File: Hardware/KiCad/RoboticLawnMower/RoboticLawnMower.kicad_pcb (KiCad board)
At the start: 2 copper layers, 100.1 x 100 mm, 117 parts, among them J1 MOTOR, J10 Conn_01x02, J11 Conn_01x02, J12 Conn_02x05_Row_Letter_Last, J13 I2C 0, J14 ADC 1, J15 ADC 2, J16 Conn_01x03, J17 Conn_01x03, J18 Conn_01x03, J19 RAIN, J2 MOTOR, J20 Dist 00, J21 Dist 01, J22 Dist 02, J3 MOTOR, J4 MOTOR, J5 MOTOR, J6 Coll 00, J7 Coll 01, J8 Coll 02, J9 GPS, Q1 BSS123, Q2 BSS123, Q3 Si7141DP, Q4 Si7141DP, U1 INA233, U10 INA233, U11 INA233, U12 INA233, U13 INA233, U2 AVR128DB48x-xPT, U3 mini_esp32, U4 PCA9685PW, U6 LT1129-3.3_SOT223, U7 TSR_1-2450, U8 ADS1115IDGS, U9 ADS1115IDGS, Y1 32.768kHz

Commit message: Layout ready add gerber file
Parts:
- removed J10: Conn_01x02, Connector_Phoenix_MC:PhoenixContact_MCV_1,5_2-GF-3.81_1x02_P3.81mm_Vertical_ThreadedFlange_MountHole
- added C11: 100n, Capacitor_SMD:C_0603_1608Metric, F.Cu at (124.2, 101.3)
- added C13: 100n, Capacitor_SMD:C_0603_1608Metric, F.Cu at (124.2, 98.6)
- added C23: 100n, Capacitor_SMD:C_0603_1608Metric, F.Cu at (124.2, 96.9)
- added C24: 100n, Capacitor_SMD:C_0603_1608Metric, F.Cu at (130.4, 101.7)
- added C34: 1u, Capacitor_SMD:C_0603_1608Metric, F.Cu at (130.4, 103.5)
- added H6: MountingHole, MountingHole:MountingHole_3.2mm_M3, F.Cu at (185.5, 80.0)
- added Q5: Si7141DP, Package_SO:PowerPAK_SO-8_Single, F.Cu at (99.1, 57.4)
- added Q6: BSS123, Package_TO_SOT_SMD:SOT-23, F.Cu at (100.7, 62.0)
- added R19: 4k7, Resistor_SMD:R_0603_1608Metric, F.Cu at (139.3, 106.2)
- added R20: 4k7, Resistor_SMD:R_0603_1608Metric, F.Cu at (137.5, 106.2)
- added R21: 4k7, Resistor_SMD:R_0603_1608Metric, F.Cu at (135.0, 106.2)
- added R22: 1K, Resistor_SMD:R_0603_1608Metric, F.Cu at (97.2, 62.0)
- added R23: 100k, Resistor_SMD:R_0603_1608Metric, F.Cu at (94.1, 58.8)
- added R24: 1M, Resistor_SMD:R_0603_1608Metric, F.Cu at (103.6, 62.0)
- added R25: 100R, Resistor_SMD:R_0603_1608Metric, F.Cu at (103.6, 65.0)
- added U5: W25Q128JVS, Package_SO:SOIC-8_5.23x5.23mm_P1.27mm, F.Cu at (136.9, 101.5)
- moved H5 47.6 mm to (92.4, 90.8)
- moved R42 16.0 mm to (127.4, 108.7)
- moved R41 15.9 mm to (127.4, 107.1)
- moved U7 14.7 mm to (95.2, 107.0)
- moved C15 4.96 mm to (105.1, 111.1)
- moved C16 4.96 mm to (105.0, 109.3)
- moved C17 4.78 mm to (105.0, 98.2)
- moved U6 4.78 mm to (103.0, 104.5)
- moved C18 4.78 mm to (105.0, 99.9)
- moved C25 3.94 mm to (140.3, 82.2), turned to 90 degrees
- moved R26 2.01 mm to (126.6, 79.1)
- moved R27 2.01 mm to (137.0, 82.2)
- moved U2 2.01 mm to (129.7, 91.8)
- moved J12 2.01 mm to (131.7, 81.4)
- moved R28 1.89 mm to (138.7, 82.2)
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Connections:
- J9 pad 7: unconnected-(J9-Pad7) -> /GPS/GPS_MOD_EN
- U2 pad 12: /i2c_io_pwm/~{PCA_9685_OE} -> /Motor_M5_EN
- U2 pad 16: /Motor_M5_EN -> /i2c_io_pwm/~{PCA_9685_OE}
- U2 pad 20: unconnected-(U2-Pad20) -> /Motor_M2/MOT_SIGNAL
- U2 pad 4: unconnected-(U2-Pad4) -> /WLAN/WLAN_MOD_EN
- U2 pad 44: unconnected-(U2-Pad44) -> /Motor_M1/MOT_SIGNAL
- U2 pad 5: unconnected-(U2-Pad5) -> /GPS/GPS_MOD_EN
- U3 pad 16: +3.3V -> Net-(U3-Pad16)
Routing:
- net +3.3V: track 160.1 -> 486.1 mm, vias 12 -> 14
- net GND: track 393.8 -> 620.9 mm, vias 10 -> 13
- net /Sensor/Collision_Sensor_00: track 0.00 -> 73.0 mm, vias 0 -> 1
- net /i2c_analog/SCL: track 4.55 -> 72.4 mm, vias 1 -> 0
- net /Sensor/Collision_Sensor_01: track 0.00 -> 64.7 mm, vias 0 -> 1
- net /Sensor/Collision_Sensor_02: track 0.00 -> 63.2 mm, vias 0 -> 1
- net /i2c_analog/SDA: track 5.48 -> 65.3 mm, vias 1 -> 0
- net /Sensor/DistanceSensor_00: track 0.00 -> 44.8 mm
- net /WLAN/WLAN_MOD_EN: track 0.00 -> 41.1 mm
- net /Sensor/RainSensor: track 0.00 -> 41.0 mm
- net /Sensor/DistanceSensor_02: track 0.00 -> 37.3 mm
- net /GPS/GPS_MOD_EN: track 0.00 -> 32.6 mm
- net /Motor_M2/MOT_SIGNAL: track 32.0 -> 62.3 mm, vias 1 -> 3
- net /Sensor/DistanceSensor_01: track 0.00 -> 28.1 mm
- net /Motor_M1/MOT_SIGNAL: track 45.7 -> 73.6 mm, vias 1 -> 3
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- added copper zone on B.Cu, net GND
- added copper zone on F.Cu, net GND
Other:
- board text added: "3V3 AIN 0 AIN 1 AIN 2 AIN 3 GND"
- board text added: "3V3 GND Sig"
- board text added: "3V3 GND TXD RXD RES PPS POW_EN"
- board text added: "3V3 SCL SDA GND"
- board text added: "DBG/PROG"
- board text added: "GPS"
- board text added: "MOTOR"
- board text added: "POWER + - 12-24V"
- board text added: "U+ GND N.C. EN SIG PWM 0 PWM 1 GND"
- board text added: "WLAN-ESP32 WEMOS D1"

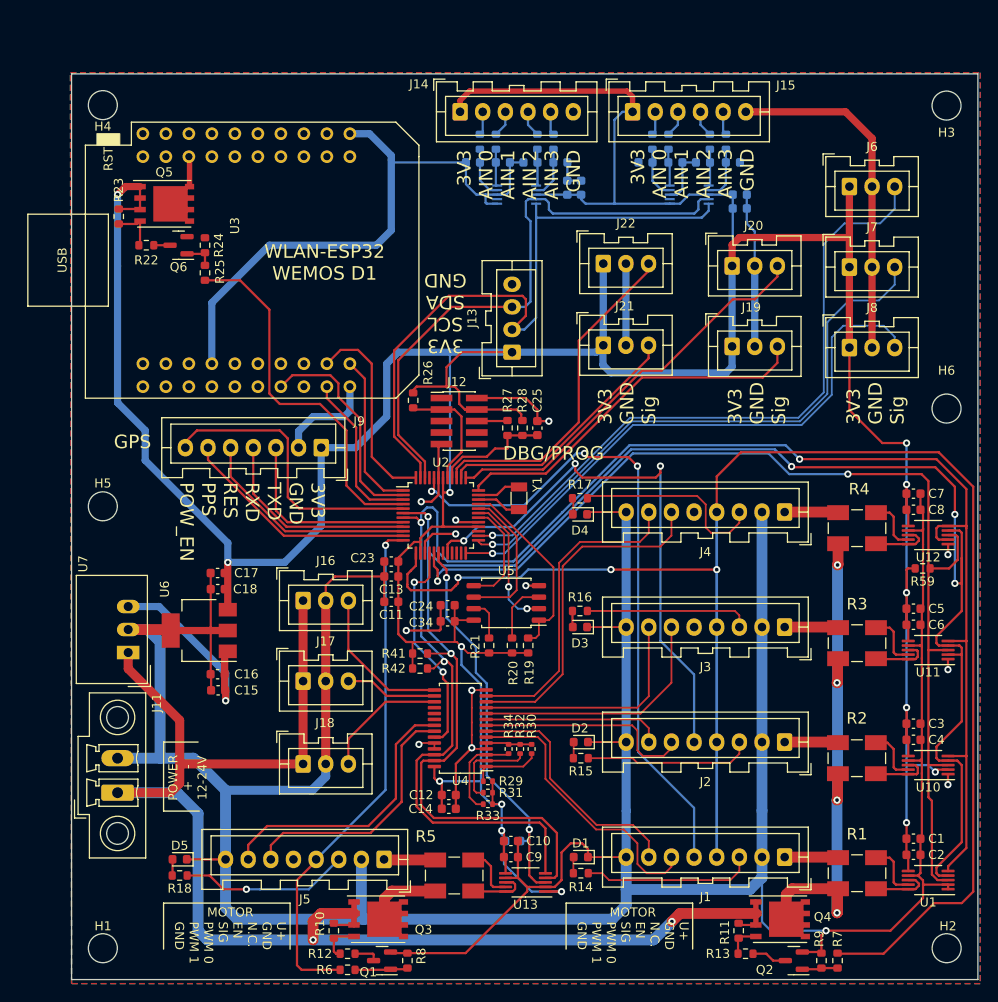
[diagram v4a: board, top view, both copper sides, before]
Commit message: Redesign: - Controller - I2C pinning geändert - uvm
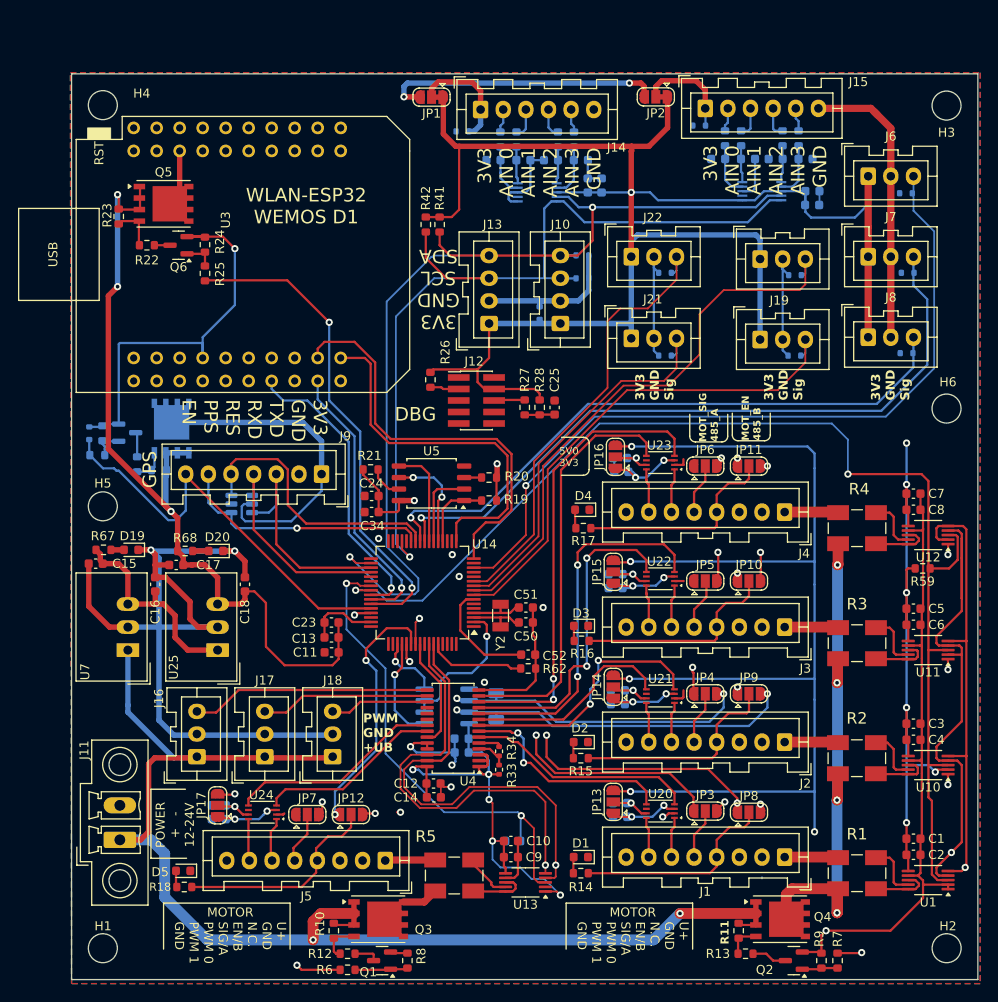
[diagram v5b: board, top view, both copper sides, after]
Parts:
- removed R29, R31: 10K, Resistor_SMD:R_0402_1005Metric
- removed R30, R32: N.P., Resistor_SMD:R_0402_1005Metric
- removed Y1: 32.768kHz, Crystal:Crystal_SMD_3215-2Pin_3.2x1.5mm
- added C35: 100n, Capacitor_SMD:C_0603_1608Metric, B.Cu at (149.5, 125.1)
- added C36: 100n, Capacitor_SMD:C_0603_1608Metric, B.Cu at (149.2, 112.6)
- added C37: 100n, Capacitor_SMD:C_0603_1608Metric, B.Cu at (149.0, 99.8)
- added C38: 100n, Capacitor_SMD:C_0603_1608Metric, B.Cu at (149.6, 87.0)
- added C39: 100n, Capacitor_SMD:C_0603_1608Metric, B.Cu at (105.2, 125.3)
- added C45: 100n, Capacitor_SMD:C_0603_1608Metric, B.Cu at (149.5, 123.6)
- added C46: 100n, Capacitor_SMD:C_0603_1608Metric, B.Cu at (149.2, 111.1)
- added C47: 100n, Capacitor_SMD:C_0603_1608Metric, B.Cu at (149.0, 98.3)
- added C48: 100n, Capacitor_SMD:C_0603_1608Metric, B.Cu at (149.5, 85.5)
- added C49: 100n, Capacitor_SMD:C_0603_1608Metric, B.Cu at (105.2, 123.8)
- added C50: Cx, Capacitor_SMD:C_0603_1608Metric, F.Cu at (139.1, 103.6)
- added C51: Cx, Capacitor_SMD:C_0603_1608Metric, F.Cu at (139.1, 102.0)
- added C52: 100n, Capacitor_SMD:C_0603_1608Metric, F.Cu at (139.3, 107.2)
- added C53: 100n, Capacitor_SMD:C_0603_1608Metric, B.Cu at (132.0, 116.5)
- added C54: 1u, Capacitor_SMD:C_0603_1608Metric, B.Cu at (132.0, 118.0)
- added D10: ESD5Zxx, Diode_SMD:D_SOD-523, B.Cu at (181.1, 73.9)
- added D11: ESD5Zxx, Diode_SMD:D_SOD-523, B.Cu at (181.2, 65.0)
- added D12: ESD5Zxx, Diode_SMD:D_SOD-523, B.Cu at (181.0, 56.2)
- added D13: ESD5Zxx, Diode_SMD:D_SOD-523, B.Cu at (132.1, 49.4)
- added D14: ESD5Zxx, Diode_SMD:D_SOD-523, B.Cu at (158.2, 48.8)
- added D15: ESD5Zxx, Diode_SMD:D_SOD-523, B.Cu at (145.3, 65.6)
- added D16: ESD5Zxx, Diode_SMD:D_SOD-523, B.Cu at (145.3, 63.1)
- added D17: ESD5Zxx, Diode_SMD:D_SOD-523, B.Cu at (140.6, 69.5)
- added D18: ESD5Zxx, Diode_SMD:D_SOD-523, B.Cu at (90.9, 82.7)
- added D19: LED_GREEN, LED_SMD:LED_0603_1608Metric, F.Cu at (95.5, 95.6)
- added D20: LED_GREEN, LED_SMD:LED_0603_1608Metric, F.Cu at (104.8, 95.7)
- added D6: ESD5Zxx, Diode_SMD:D_SOD-523, B.Cu at (168.7, 74.2)
- added D7: ESD5Zxx, Diode_SMD:D_SOD-523, B.Cu at (168.8, 65.3)
- added D8: ESD5Zxx, Diode_SMD:D_SOD-523, B.Cu at (154.4, 74.2)
- added D9: ESD5Zxx, Diode_SMD:D_SOD-523, B.Cu at (154.4, 65.0)
- added J10: I2C 0, Connector_JST:JST_XA_B04B-XASK-1_1x04_P2.50mm_Vertical, F.Cu at (142.9, 70.6)
- added JP1: Jumper_3_Open, Jumper:SolderJumper-3_P1.3mm_Bridged12_RoundedPad1.0x1.5mm, F.Cu at (128.7, 45.6)
- added JP10: SolderJumper_3_Open, Jumper:SolderJumper-3_P1.3mm_Open_RoundedPad1.0x1.5mm, F.Cu at (163.7, 99.1)
- added JP11: SolderJumper_3_Open, Jumper:SolderJumper-3_P1.3mm_Open_RoundedPad1.0x1.5mm, F.Cu at (163.7, 86.4)
- added JP12: SolderJumper_3_Open, Jumper:SolderJumper-3_P1.3mm_Open_RoundedPad1.0x1.5mm, F.Cu at (119.8, 124.8)
- added JP13: SolderJumper_3_Open, Jumper:SolderJumper-3_P1.3mm_Open_RoundedPad1.0x1.5mm, F.Cu at (148.7, 123.4)
- added JP14: SolderJumper_3_Open, Jumper:SolderJumper-3_P1.3mm_Open_RoundedPad1.0x1.5mm, F.Cu at (148.7, 110.7)
- added JP15: SolderJumper_3_Open, Jumper:SolderJumper-3_P1.3mm_Open_RoundedPad1.0x1.5mm, F.Cu at (148.7, 98.0)
- added JP16: SolderJumper_3_Open, Jumper:SolderJumper-3_P1.3mm_Open_RoundedPad1.0x1.5mm, F.Cu at (149.0, 85.3)
- added JP17: SolderJumper_3_Open, Jumper:SolderJumper-3_P1.3mm_Open_RoundedPad1.0x1.5mm, F.Cu at (105.0, 123.8)
- added JP2: Jumper_3_Open, Jumper:SolderJumper-3_P1.3mm_Bridged12_RoundedPad1.0x1.5mm, F.Cu at (153.4, 45.6)
- added JP3: SolderJumper_3_Open, Jumper:SolderJumper-3_P1.3mm_Open_RoundedPad1.0x1.5mm, F.Cu at (158.9, 124.5)
- added JP4: SolderJumper_3_Open, Jumper:SolderJumper-3_P1.3mm_Open_RoundedPad1.0x1.5mm, F.Cu at (158.9, 111.5)
- added JP5: SolderJumper_3_Open, Jumper:SolderJumper-3_P1.3mm_Open_RoundedPad1.0x1.5mm, F.Cu at (158.9, 99.1)
- added JP6: SolderJumper_3_Open, Jumper:SolderJumper-3_P1.3mm_Open_RoundedPad1.0x1.5mm, F.Cu at (158.9, 86.4)
- added JP7: SolderJumper_3_Open, Jumper:SolderJumper-3_P1.3mm_Open_RoundedPad1.0x1.5mm, F.Cu at (114.9, 124.8)
- added JP8: SolderJumper_3_Open, Jumper:SolderJumper-3_P1.3mm_Open_RoundedPad1.0x1.5mm, F.Cu at (163.7, 124.6)
- added JP9: SolderJumper_3_Open, Jumper:SolderJumper-3_P1.3mm_Open_RoundedPad1.0x1.5mm, F.Cu at (163.7, 111.5)
- added Q7: Si7141DP, Package_SO:PowerPAK_SO-8_Single, B.Cu at (99.9, 82.2)
- added Q8: BSS123, Package_TO_SOT_SMD:SOT-23, B.Cu at (95.0, 82.7)
- added R62: 47K, Resistor_SMD:R_0603_1608Metric, F.Cu at (139.3, 108.7)
- added R63: 1K, Resistor_SMD:R_0603_1608Metric, B.Cu at (96.1, 86.2)
- added R64: 100k, Resistor_SMD:R_0603_1608Metric, B.Cu at (98.6, 86.8)
- added R65: 1M, Resistor_SMD:R_0603_1608Metric, B.Cu at (92.3, 82.7)
- added R66: 100R, Resistor_SMD:R_0603_1608Metric, B.Cu at (91.7, 85.2)
- added R67: 4k7, Resistor_SMD:R_0603_1608Metric, F.Cu at (92.4, 95.6)
- added R68: 4k7, Resistor_SMD:R_0603_1608Metric, F.Cu at (101.4, 95.7)
- added R69: 120, Resistor_SMD:R_1206_3216Metric, B.Cu at (135.8, 112.9)
- added U14: STM32H503RBTx, Package_QFP:LQFP-64_10x10mm_P0.5mm, F.Cu at (127.6, 100.3)
- added U20: TXB0102DCU, Package_SO:VSSOP-8_2.4x2.1mm_P0.5mm, F.Cu at (153.9, 124.5)
- added U21: TXB0102DCU, Package_SO:VSSOP-8_2.4x2.1mm_P0.5mm, F.Cu at (153.9, 111.8)
- added U22: TXB0102DCU, Package_SO:VSSOP-8_2.4x2.1mm_P0.5mm, F.Cu at (153.9, 98.8)
- added U23: TXB0102DCU, Package_SO:VSSOP-8_2.4x2.1mm_P0.5mm, F.Cu at (153.9, 86.0)
- added U24: TXB0102DCU, Package_SO:VSSOP-8_2.4x2.1mm_P0.5mm, F.Cu at (110.0, 124.6)
- added U25: TSR_1-2450, Converter_DCDC:Converter_DCDC_TRACO_TSR-1_THT, F.Cu at (105.0, 106.7)
- added Y2: 32.768kHz, Crystal:Crystal_SMD_3215-2Pin_3.2x1.5mm, F.Cu at (136.3, 102.9)
- R33: value 10K -> N.P.
- R34: value N.P. -> 0R0
- U2: value AVR128DB48x-xPT -> LT1785AxS8; footprint Package_QFP:TQFP-48_7x7mm_P0.5mm -> Package_SO:SOIC-8_3.9x4.9mm_P1.27mm; moved to B.Cu
- U6: value LT1129-3.3_SOT223 -> SRV05-4; footprint Package_TO_SOT_SMD:SOT-223-3_TabPin2 -> Package_TO_SOT_SMD:SOT-23-6; moved to B.Cu
- moved R42 49.0 mm to (128.0, 59.7), turned to 90 degrees
- moved R41 47.4 mm to (129.5, 59.7), turned to 90 degrees
- moved R21 23.4 mm to (121.9, 86.7), turned to 180 degrees
- moved U2 21.1 mm to (130.3, 112.9)
- moved J16 20.8 mm to (102.7, 118.5), turned to 90 degrees
- moved C15 19.5 mm to (91.6, 97.1)
- moved R20 18.7 mm to (135.0, 87.6), turned to 0 degrees
- moved R19 16.6 mm to (135.0, 90.2), turned to 0 degrees
- moved U5 15.6 mm to (128.7, 88.3)
- moved U6 14.7 mm to (107.7, 90.6), turned to 0 degrees
- moved C24 14.7 mm to (122.0, 89.7)
- moved C34 14.7 mm to (122.0, 91.4)
- moved C16 12.1 mm to (98.1, 99.4), turned to 90 degrees
- moved C23 9.43 mm to (117.6, 103.6)
- moved C13 9.43 mm to (117.6, 105.3)
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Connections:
- J1 pad 4: /Motor_M1..4_EN -> Net-(J1-Pin_4)
- J1 pad 5: /Motor_M1/MOT_SIGNAL -> Net-(J1-Pin_5)
- J1 pad 6: /PWM_CH_0 -> Net-(J1-Pin_6)
- J1 pad 7: /PWM_CH_1 -> Net-(J1-Pin_7)
- J13 pad 2: /i2c_analog/SCL -> GND
- J13 pad 3: /i2c_analog/SDA -> /i2c_analog/I2C_2_SCL
- J13 pad 4: GND -> /i2c_analog/I2C_2_SDA
- J14 pad 1: +3.3V -> Net-(D13-K)
- J15 pad 1: +3.3V -> Net-(D14-K)
- J2 pad 4: /Motor_M1..4_EN -> Net-(J2-Pin_4)
- J2 pad 5: /Motor_M2/MOT_SIGNAL -> Net-(J2-Pin_5)
- J2 pad 6: /PWM_CH_2 -> Net-(J2-Pin_6)
- J2 pad 7: /PWM_CH_3 -> Net-(J2-Pin_7)
- J3 pad 4: /Motor_M1..4_EN -> Net-(J3-Pin_4)
- J3 pad 5: /Motor_M3/MOT_SIGNAL -> Net-(J3-Pin_5)
- J3 pad 6: /PWM_CH_4 -> Net-(J3-Pin_6)
- J3 pad 7: /PWM_CH_5 -> Net-(J3-Pin_7)
- J4 pad 4: /Motor_M1..4_EN -> Net-(J4-Pin_4)
- J4 pad 5: /Motor_M4/MOT_SIGNAL -> Net-(J4-Pin_5)
- J4 pad 6: /PWM_CH_6 -> Net-(J4-Pin_6)
- J4 pad 7: /PWM_CH_7 -> Net-(J4-Pin_7)
- J5 pad 4: /Motor_M5_EN -> Net-(J5-Pin_4)
- J5 pad 5: /Motor_M5/MOT_SIGNAL -> Net-(J5-Pin_5)
- J5 pad 6: /PWM_CH_15 -> Net-(J5-Pin_6)
- J5 pad 7: /PWM_CH_14 -> Net-(J5-Pin_7)
- J6 pad 3: /Sensor/Collision_Sensor_00 -> /uC/ADC_1_IN0
- J7 pad 3: /Sensor/Collision_Sensor_01 -> /uC/ADC_1_IN4
- J8 pad 3: /Sensor/Collision_Sensor_02 -> /uC/ADC_1_IN8
- J9 pad 1: +3.3V -> Net-(J9-Pin_1)
- J9 pad 3: /GPS/GPS_UART_3_TXD -> /uC/USART_1_TX
- J9 pad 4: /GPS/GPS_UART_3_RXD -> /uC/USART_1_RX
- R14 pad 1: /Motor_M1/MOT_5V_OUT -> Net-(J1-Pin_4)
- R15 pad 1: /Motor_M2/MOT_5V_OUT -> Net-(J2-Pin_4)
- R16 pad 1: /Motor_M3/MOT_5V_OUT -> Net-(J3-Pin_4)
- R17 pad 1: /Motor_M4/MOT_5V_OUT -> Net-(J4-Pin_4)
- R18 pad 1: /Motor_M5/MOT_5V_OUT -> Net-(J5-Pin_4)
- R19 pad 1: /uC/SPI_0_CS -> /uC/SPI_1_CS
- R33 pad 2: Net-(R33-Pad2) -> Net-(U4-A3)
- R34 pad 1: Net-(R33-Pad2) -> Net-(U4-A3)
- R41 pad 1: /Motor_M1/SDA -> /i2c_analog/I2C_2_SDA
- R42 pad 1: /Motor_M1/SCL -> /i2c_analog/I2C_2_SCL
- U2 pad 1: /WLAN/WLAN_TxD -> /uC/USART_3_RX
- U2 pad 2: /WLAN/UART_0_XCK -> /RS485/RS485_DIR
- U2 pad 3: /WLAN/UART_0_XDIR -> /RS485/RS485_DIR
- U2 pad 4: /WLAN/WLAN_MOD_EN -> /uC/USART_3_TX
- U2 pad 5: /GPS/GPS_MOD_EN -> GND
- U2 pad 6: /Motor_M1/SDA -> /RS485_A
- U2 pad 7: /Motor_M1/SCL -> /RS485_B
- U2 pad 8: /GPS/GPS_UART_3_TXD -> +3.3V
- U3 pad 21: /WLAN/WLAN_TxD -> /uC/USART_2_RX
- U3 pad 23: /WLAN/WLAN_RxD -> /uC/USART_2_TX
- U4 pad 1: Net-(R29-Pad2) -> +3.3V
- U4 pad 2: Net-(R31-Pad2) -> +3.3V
- U4 pad 3: Net-(R33-Pad2) -> +3.3V
- U4 pad 4: GND -> Net-(U4-A3)
- U5 pad 1: /uC/SPI_0_CS -> /uC/SPI_1_CS
- U5 pad 2: /uC/SPI_0_MISO -> /uC/SPI_1_MISO
- U5 pad 5: /uC/SPI_0_MOSI -> /uC/SPI_1_MOSI
- U5 pad 6: /uC/SPI_0_SCLK -> /uC/SPI_1_SCK
- U6 pad 1: +5V -> /GPS/GPS_PPS
- U6 pad 3: +3.3V -> /GPS/GPS_RESET_EN
- U8 pad 10: /i2c_analog/SCL -> /i2c_analog/I2C_2_SCL
- U8 pad 9: /i2c_analog/SDA -> /i2c_analog/I2C_2_SDA
- U9 pad 10: /i2c_analog/SCL -> /i2c_analog/I2C_2_SCL
- U9 pad 9: /i2c_analog/SDA -> /i2c_analog/I2C_2_SDA
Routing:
- net +5V: track 22.4 -> 363.8 mm, vias 1 -> 9
- net GND: track 620.9 -> 357.4 mm, vias 13 -> 16
- net /i2c_analog/I2C_2_SDA: track 0.00 -> 109.6 mm, vias 0 -> 2
- net /RS485_B: track 0.00 -> 104.4 mm, vias 0 -> 6
- net /RS485_A: track 0.00 -> 100.9 mm, vias 0 -> 6
- net /i2c_analog/I2C_2_SCL: track 0.00 -> 97.9 mm, vias 0 -> 1
- net /uC/ADC_1_IN0: track 0.00 -> 85.3 mm, vias 0 -> 1
- net /uC/ADC_1_IN4: track 0.00 -> 78.2 mm, vias 0 -> 1
- net /Sensor/Collision_Sensor_00: track 73.0 -> 0.00 mm, vias 1 -> 0
- net /i2c_analog/SCL: track 72.4 -> 0.00 mm
- net /uC/ADC_1_IN8: track 0.00 -> 69.0 mm, vias 0 -> 1
- net /i2c_analog/SDA: track 65.3 -> 0.00 mm
- net /Sensor/Collision_Sensor_01: track 64.7 -> 0.00 mm, vias 1 -> 0
- net /Sensor/Collision_Sensor_02: track 63.2 -> 0.00 mm, vias 1 -> 0
- net /Motor_M1..4_EN: track 175.3 -> 124.7 mm, vias 3 -> 7
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- added copper zone on In1.Cu, net +3.3V
- added copper zone on In2.Cu, net GND
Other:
- copper layers 2 -> 4
- board text added: "3V3 GND SCL SDA"
- board text added: "3V3 GND TXD RXD RES PPS EN"
- board text added: "5V0 3V3"
- board text added: "DBG"
- board text added: "MOT_EN 485_B"
- board text added: "MOT_SIG 485_A"
- board text added: "PWM GND +UB"
- board text added: "U+ GND N.C. EN/B SIG/A PWM 0 PWM 1 GND"
- board text removed: "3V3 GND TXD RXD RES PPS POW_EN"
- board text removed: "3V3 SCL SDA GND"
- board text removed: "DBG/PROG"
- board text removed: "U+ GND N.C. EN SIG PWM 0 PWM 1 GND"

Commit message: change µC to STM32H573
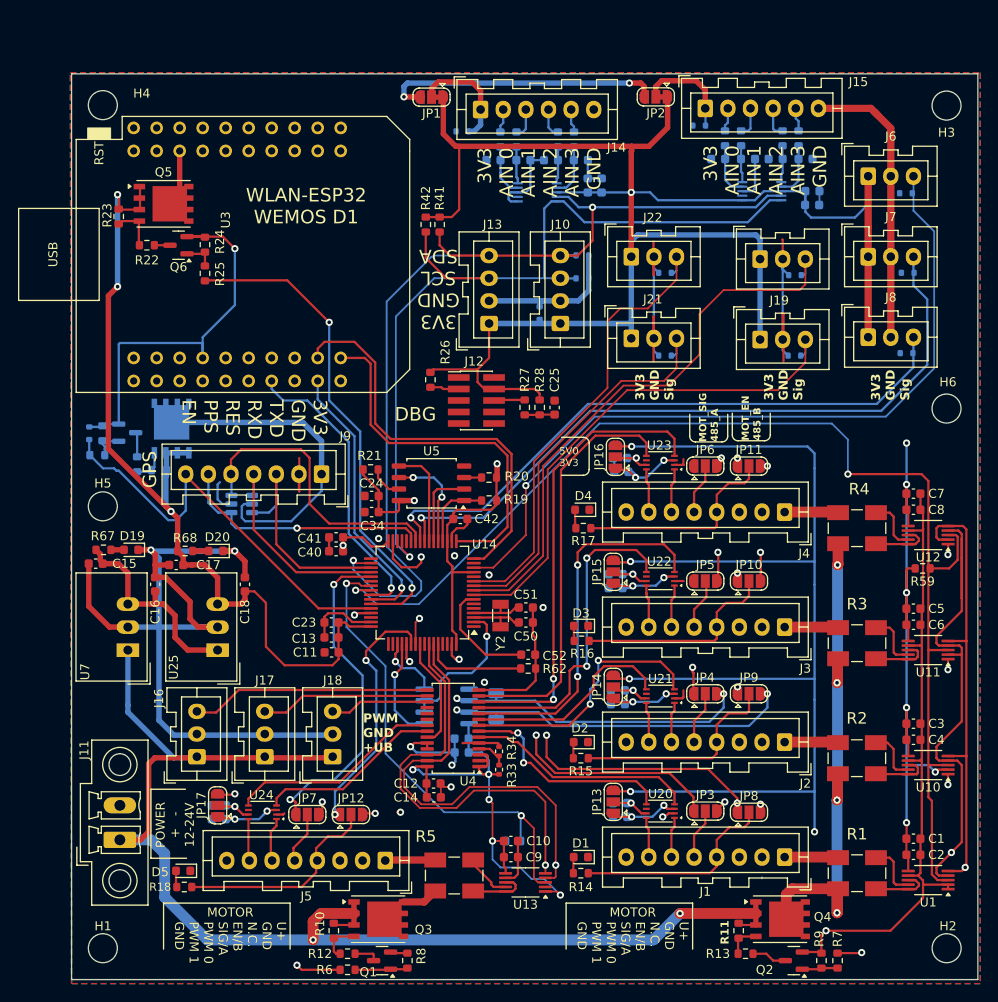
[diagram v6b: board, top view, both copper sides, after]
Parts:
- added C40: 100n, Capacitor_SMD:C_0603_1608Metric, F.Cu at (118.1, 95.8)
- added C41: 10µ, Capacitor_SMD:C_0603_1608Metric, F.Cu at (118.1, 94.2)
- added C42: 10µ, Capacitor_SMD:C_0603_1608Metric, F.Cu at (131.8, 92.2)
- U14: value STM32H503RBTx -> STM32H573RITx
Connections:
- JP7 pad 1: /Motor_M5/MOT_SIGNAL -> /MOT_SIG_5
- U14 pad 13: unconnected-(U14-VDDA-Pad13) -> +3.3V
- U14 pad 19: unconnected-(U14-VDD-Pad19) -> +3.3V
- U14 pad 32: unconnected-(U14-VDD-Pad32) -> +3.3V
- U14 pad 37: unconnected-(U14-PC6-Pad37) -> /MOT_SIG_5
- U14 pad 48: unconnected-(U14-VDD-Pad48) -> +3.3V
- U14 pad 64: unconnected-(U14-VDD-Pad64) -> +3.3V
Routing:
- net GND: track 357.4 -> 405.9 mm, vias 16 -> 18
- net /MOT_SIG_5: track 0.00 -> 36.5 mm, vias 0 -> 2
- net +3.3V: track 519.5 -> 555.0 mm, vias 27 -> 28
- net /GPS/GPS_RESET_EN: track 30.7 -> 32.6 mm
- net /Sensor/DistanceSensor_02: track 50.0 -> 51.1 mm
- net /Sensor/DistanceSensor_00: track 62.8 -> 64.0 mm
- net /Sensor/RainSensor: track 56.5 -> 57.6 mm
- net /Sensor/DistanceSensor_01: track 42.7 -> 43.8 mm
- net /Motor_M5_EN: track 52.1 -> 51.4 mm
- net Net-(U14-BOOT0): track 10.7 -> 11.3 mm

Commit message: Layout fertig, Gerber-Datei muss noch erzeugt werden.
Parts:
- removed C25: 5p6, Capacitor_SMD:C_0603_1608Metric
- removed R26, R28: 47K, Resistor_SMD:R_0603_1608Metric
- removed R27: 33R, Resistor_SMD:R_0603_1608Metric
- moved J12 0.51 mm to (133.6, 79.6)
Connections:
- C52 pad 1: Net-(U14-NRST) -> /uC/NRST
- J12 pad 1: unconnected-(J12-Pin_1-Pad1) -> +3.3V
- J12 pad 10: unconnected-(J12-Pin_10-Pad10) -> /uC/NRST
- J12 pad 2: GND -> /uC/SWDIO
- J12 pad 3: /uC/AVR_UPDI -> GND
- J12 pad 4: +3.3V -> /uC/SWCLK
- J12 pad 5: unconnected-(J12-Pin_5-Pad5) -> GND
- J12 pad 6: Net-(J12-Pin_6) -> /uC/SWO
- U14 pad 33: unconnected-(U14-PB12-Pad33) -> /i2c_analog/I2C_2_SDA
- U14 pad 34: /i2c_analog/I2C_2_SDA -> unconnected-(U14-PB13-Pad34)
- U14 pad 45: /Motor_M1/MOT_SIGNAL -> /Motor_M5_EN
- U14 pad 50: unconnected-(U14-PA15(JTDI)-Pad50) -> /Motor_M1/MOT_SIGNAL
- U14 pad 54: /Motor_M5_EN -> unconnected-(U14-PD2-Pad54)
- U14 pad 55: /Motor_M1..4_EN -> /uC/SWO
- U14 pad 57: unconnected-(U14-PB5-Pad57) -> /Motor_M1..4_EN
- U14 pad 7: Net-(U14-NRST) -> /uC/NRST
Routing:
- net /uC/SWCLK: track 0.00 -> 39.9 mm, vias 0 -> 2
- net /uC/NRST: track 0.00 -> 39.6 mm, vias 0 -> 2
- net /uC/SWDIO: track 0.00 -> 39.2 mm, vias 0 -> 2
- net /uC/SWO: track 0.00 -> 37.0 mm, vias 0 -> 2
- net +3.3V: track 555.0 -> 541.0 mm, vias 28 -> 29
- net Net-(U14-NRST): track 12.3 -> 0.00 mm
- net /Motor_M1/MOT_SIGNAL: track 51.7 -> 46.0 mm
- net Net-(J12-Pin_6): track 3.41 -> 0.00 mm
- net /uC/~{AVR_RERSET}: track 3.32 -> 0.00 mm
- net /uC/AVR_UPDI: track 3.21 -> 0.00 mm
- net /Motor_M1..4_EN: track 124.7 -> 122.9 mm
- net /Motor_M5_EN: track 51.4 -> 50.8 mm, vias 3 -> 4
- net GND: vias 18 -> 19
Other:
- board text added: "AIN0"
- board text added: "AIN4"
- board text added: "AIN8"
- board text added: "ANALOG"
- board text added: "MOTOR 1"
- board text added: "MOTOR 2"
- board text added: "MOTOR 3"
- board text added: "MOTOR 4"
- board text added: "MOTOR M"
